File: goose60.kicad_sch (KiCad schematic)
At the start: 33 parts

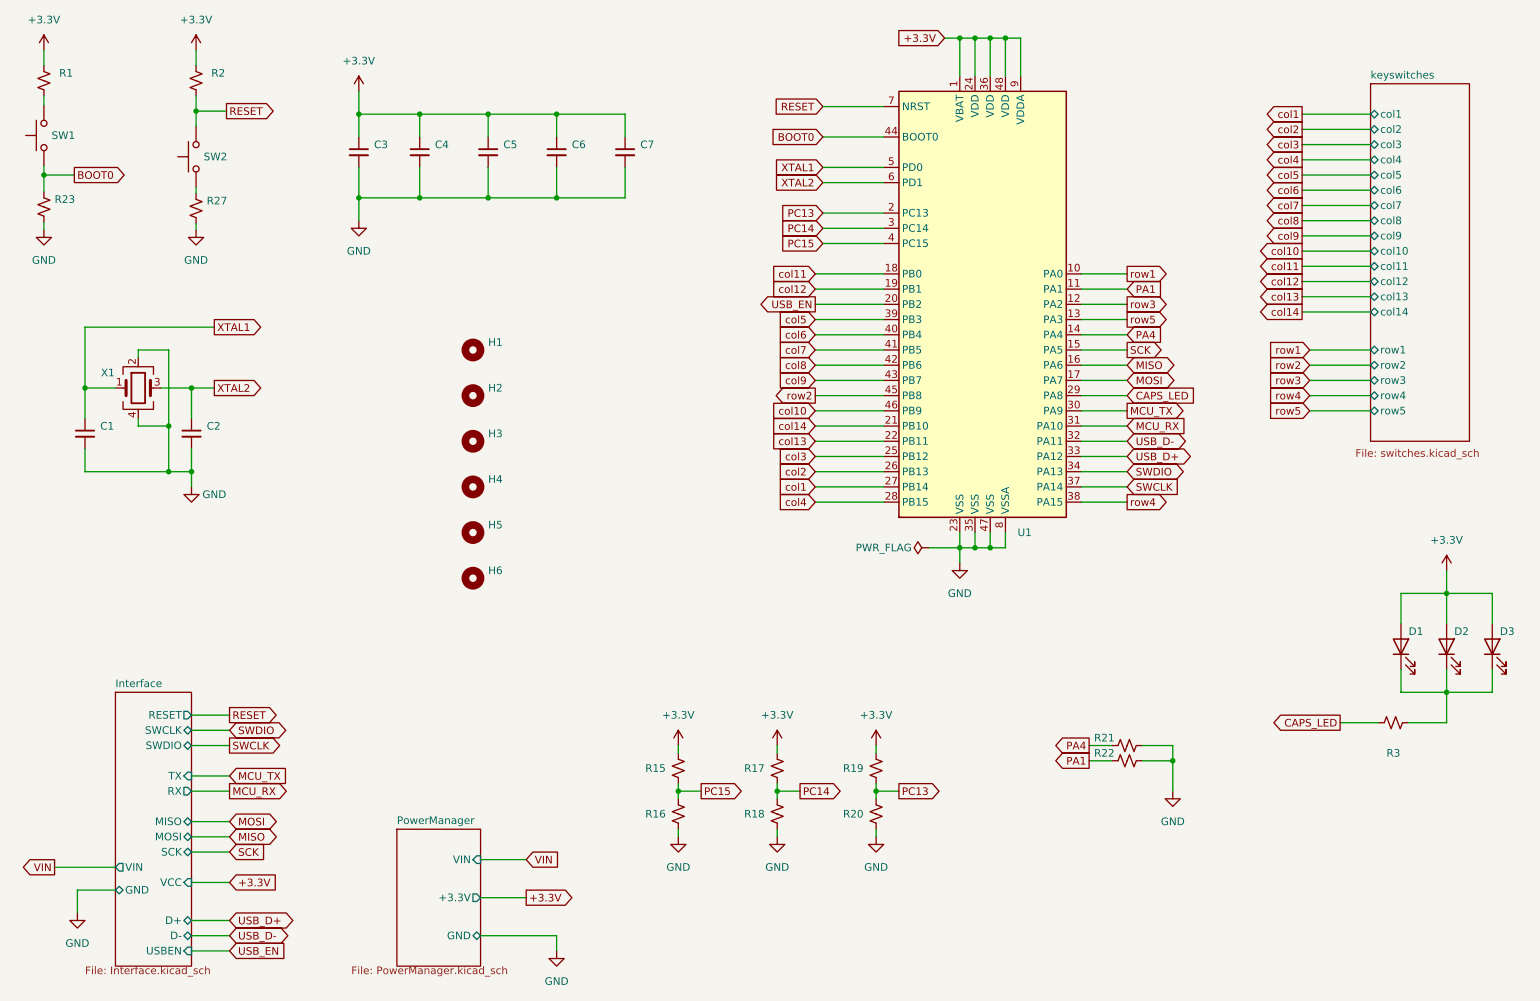
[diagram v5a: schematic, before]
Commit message: change Diode direction and update PR #1 footprint
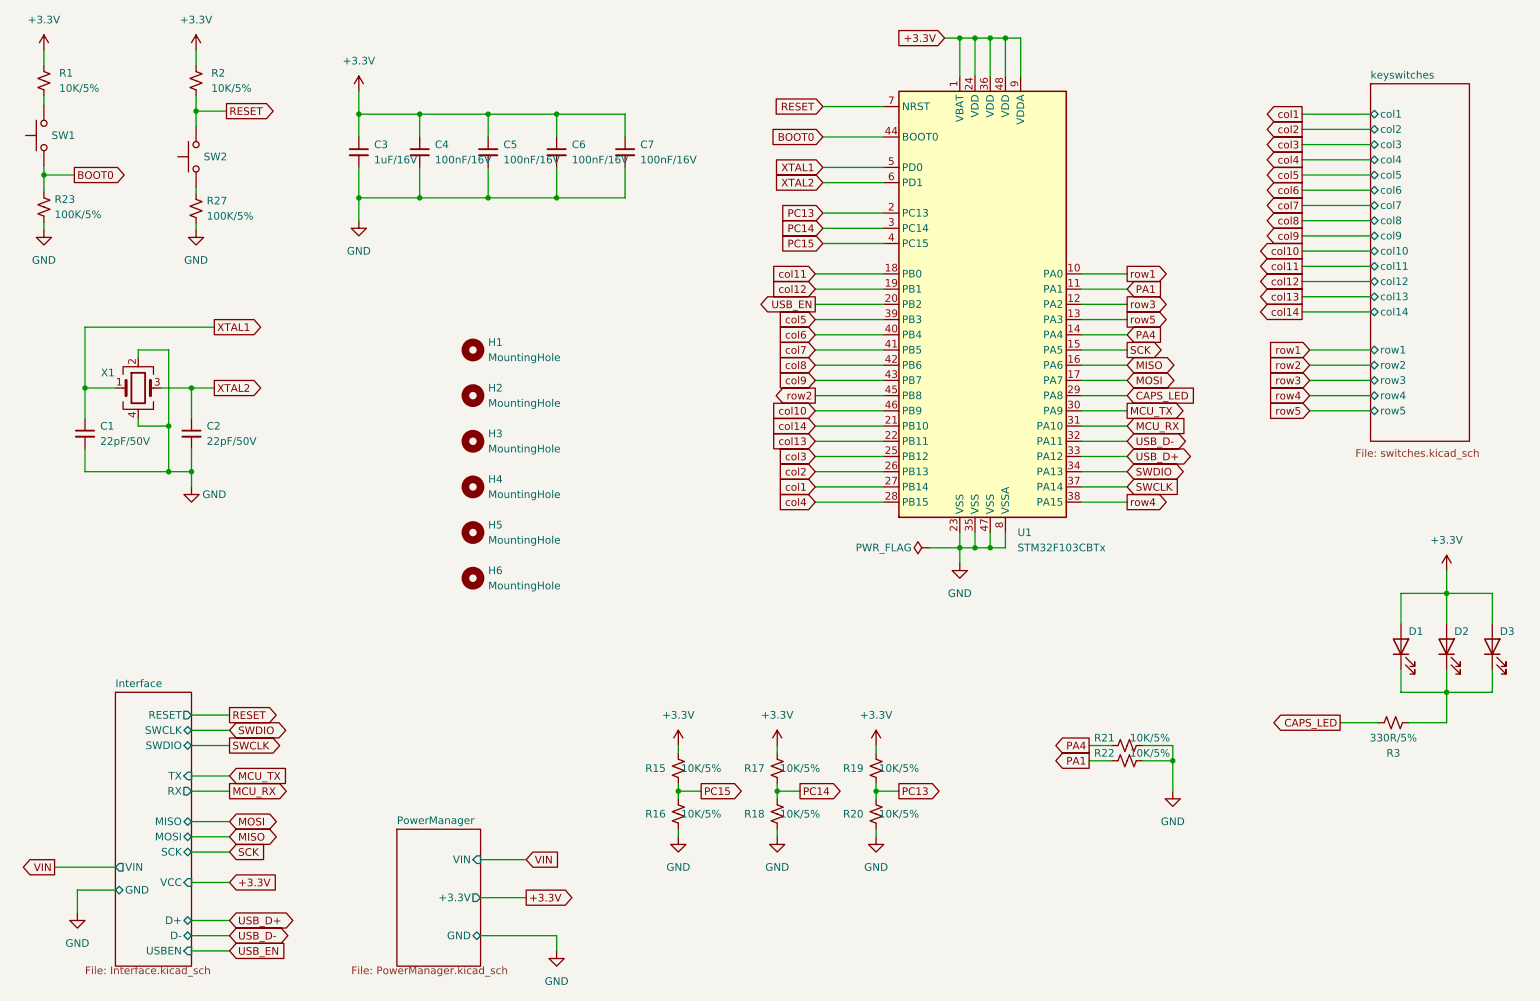
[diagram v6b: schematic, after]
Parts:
- C1, C2: value (none) -> 22pF/50V; footprint (none) -> Capacitor_SMD:C_0603_1608Metric
- C3: value (none) -> 1uF/16V; footprint (none) -> Capacitor_SMD:C_0603_1608Metric
- C4, C5, C6, C7: value (none) -> 100nF/16V; footprint (none) -> Capacitor_SMD:C_0603_1608Metric
- D1, D2, D3: value (none) -> LED; footprint (none) -> LED_SMD:LED_0805_2012Metric
- H1: value (none) -> MountingHole; footprint (none) -> MountingHole:MountingHole_3.2mm_M3_Pad
- H2, H3, H4, H5, H6: value (none) -> MountingHole; footprint (none) -> MountingHole:MountingHole_3.2mm_M3_Pad_TopOnly
- R1, R15, R16, R17, R18, R19, R2, R20, R21, R22: value (none) -> 10K/5%; footprint (none) -> Resistor_SMD:R_0603_1608Metric
- R23, R27: value (none) -> 100K/5%; footprint (none) -> Resistor_SMD:R_0603_1608Metric
- R3: value (none) -> 330R/5%; footprint (none) -> Resistor_SMD:R_0603_1608Metric
- SW1, SW2: value (none) -> SW_Push; footprint (none) -> Button_Switch_SMD:SW_Push_1P1T_NO_CK_KSC6xxJ
- U1: value (none) -> STM32F103CBTx; footprint (none) -> Package_QFP:LQFP-48_7x7mm_P0.5mm
- X1: value (none) -> Crystal_GND24; footprint (none) -> Crystal:Crystal_SMD_TXC_7M-4Pin_3.2x2.5mm

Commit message: update pcb layout
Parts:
- removed D2, D3: LED, LED_SMD:LED_0805_2012Metric, symbol Device:LED
- removed R16, R18, R20: 10K/5%, Resistor_SMD:R_0603_1608Metric, symbol Device:R_Small_US
- added R11: 10K/5%, Resistor_SMD:R_0603_1608Metric, symbol Device:R_Small_US
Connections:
- net GND: now also R11.1
- net USB_EN renamed PB2
- net PB2: now also R11.2
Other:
- sheet Interface ports: added none; removed USBEN
- moved on the sheet: D1, R21, R22

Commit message: update pcb layout and add GND via
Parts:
- H1: footprint MountingHole:MountingHole_3.2mm_M3_Pad -> MountingHole:MountingHole_3.2mm_M3_Pad_TopOnly
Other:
- moved on the sheet: H4
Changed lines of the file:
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@@
     (pin "2")
   )
-  (symbol (lib_id "Mechanical:MountingHole") (at 99.06 100.33 0) (unit 1)
-    (in_bom yes) (on_board yes) (fields_autoplaced)
-    (property "Reference" "H4" (id 0) (at 101.6 99.0599 0)
-      (effects (font (size 1.27 1.27)) (justify left))
-    )
-    (property "Value" "MountingHole" (id 1) (at 101.6 101.5999 0)
-      (effects (font (size 1.27 1.27)) (justify left))
+  (symbol (lib_id "Mechanical:MountingHole") (at 99.06 100.33 90) (unit 1)
+    (in_bom yes) (on_board yes) (fields_autoplaced)
+    (property "Reference" "H4" (id 0) (at 101.6 99.0599 90)
+      (effects (font (size 1.27 1.27)) (justify right))
+    )
+    (property "Value" "MountingHole" (id 1) (at 101.6 101.5999 90)
+      (effects (font (size 1.27 1.27)) (justify right))
     )
     (property "Footprint" "MountingHole:MountingHole_3.2mm_M3_Pad_TopOnly" (id 2) (at 99.06 100.33 0)
@@
       (effects (font (size 1.27 1.27)) (justify left))
     )
-    (property "Footprint" "MountingHole:MountingHole_3.2mm_M3_Pad" (id 2) (at 99.06 77.47 0)
+    (property "Footprint" "MountingHole:MountingHole_3.2mm_M3_Pad_TopOnly" (id 2) (at 99.06 77.47 0)
       (effects (font (size 1.27 1.27)) hide)
     )
@@
     )
     (path "/e5255316-baa4-4e6b-b2de-4b7fd45b19cb"
-      (reference "H1") (unit 1) (value "MountingHole") (footprint "MountingHole:MountingHole_3.2mm_M3_Pad")
+      (reference "H1") (unit 1) (value "MountingHole") (footprint "MountingHole:MountingHole_3.2mm_M3_Pad_TopOnly")
     )
     (path "/b34b0885-1966-40a8-9043-234e7293b68d"
